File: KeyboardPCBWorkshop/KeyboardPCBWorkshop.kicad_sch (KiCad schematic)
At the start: 1 part, among them U1 ATmega32U4-A

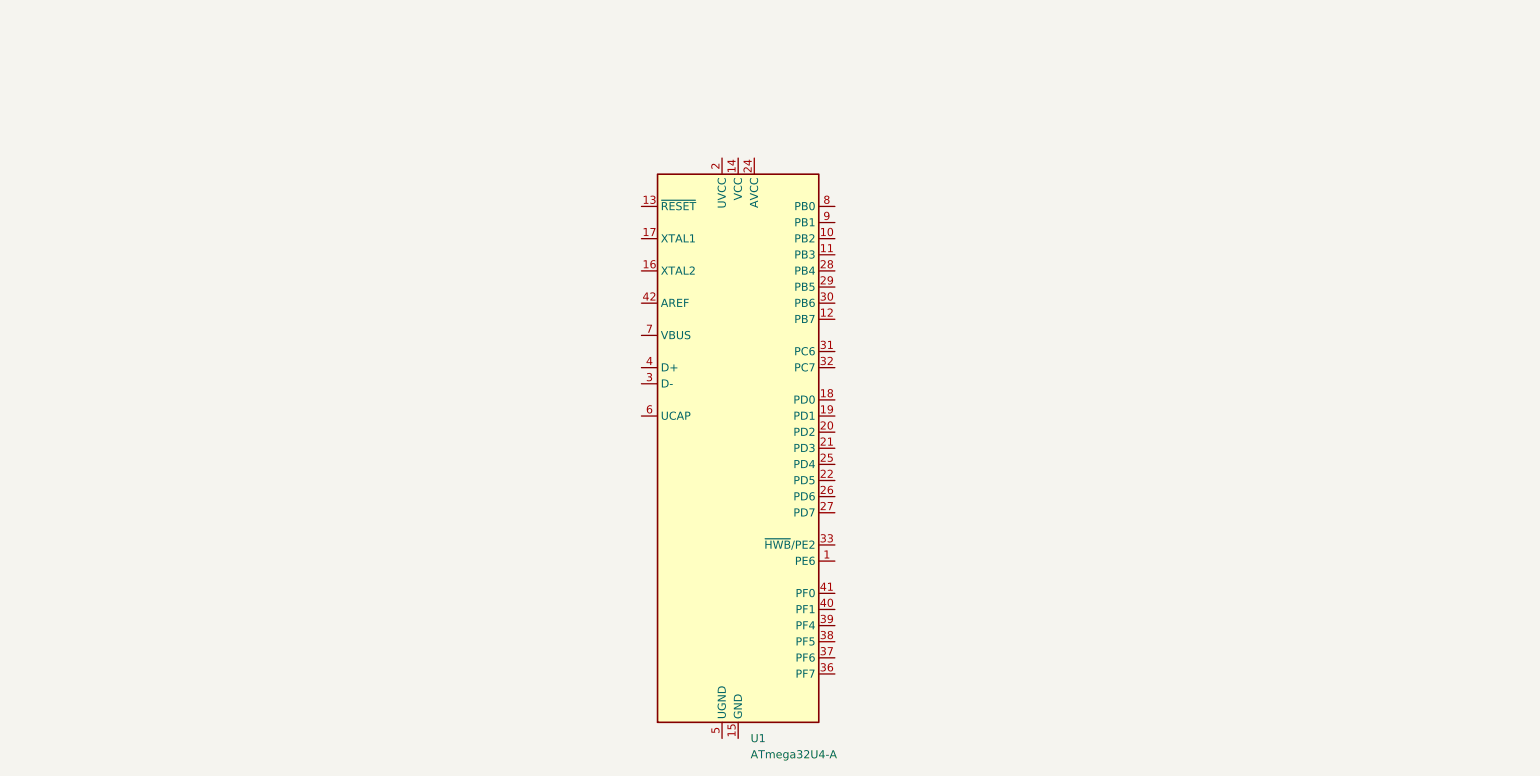
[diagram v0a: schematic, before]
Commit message: added XTAL, coupling cap, ISP header
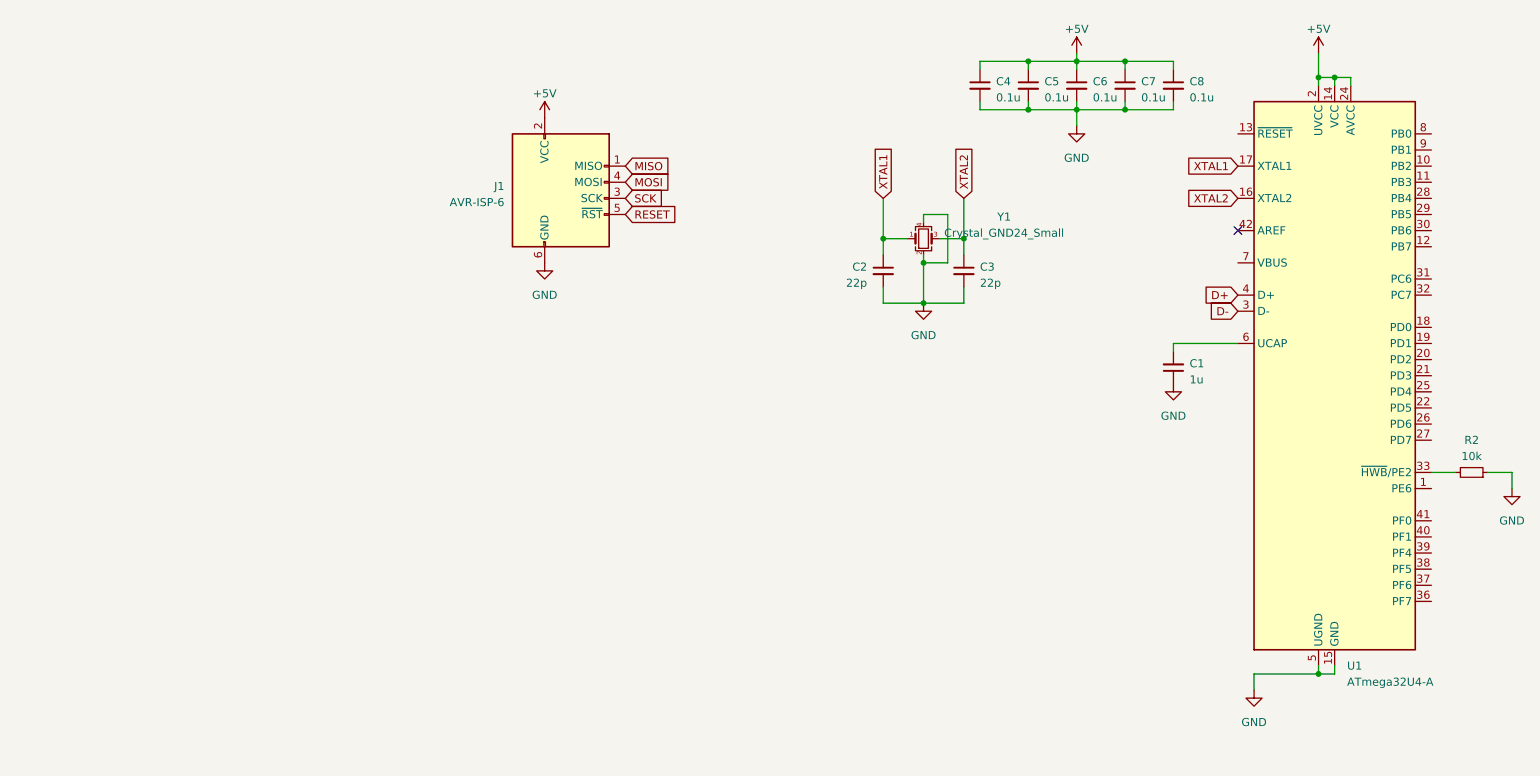
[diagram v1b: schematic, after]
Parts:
- added C1: 1u, symbol Device:C_Small
- added C2, C3: 22p, symbol Device:C_Small
- added C4, C5, C6, C7, C8: 0.1u, symbol Device:C_Small
- added J1: AVR-ISP-6, symbol Connector:AVR-ISP-6
- added R2: 10k, symbol Device:R_Small
- added Y1: Crystal_GND24_Small, symbol Device:Crystal_GND24_Small
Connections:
- net +5V: now reaches U1.14 (VCC), U1.34 (VCC)
- net +5V: now also U1.2 (UVCC), U1.24 (AVCC), U1.44 (AVCC), C4.1, C5.1, C6.1, C7.1, C8.1, J1.2 (VCC)
- net GND: now reaches U1.15 (GND), U1.23 (GND), U1.35 (GND), U1.43 (GND)
- net GND: now also U1.5 (UGND), C1.1, C2.2, C3.2, C4.2, C5.2, C6.2, C7.2, C8.2, J1.6 (GND), R2.1, Y1.2, Y1.4
- net XTAL2: now reaches U1.16 (XTAL2)
- net XTAL2: now also C3.1, Y1.3
- net XTAL1: now reaches U1.17 (XTAL1)
- net XTAL1: now also C2.1, Y1.1
- net D-: now reaches U1.3 (D-)
- net at U1.33 (~{HWB}/PE2): now also R2.2
- net D+: now reaches U1.4 (D+)
- net at U1.6 (UCAP): now also C1.2
- new net MISO: J1.1 (MISO)
- new net MOSI: J1.4 (MOSI)
- new net RESET: J1.5 (~{RST})
- new net SCK: J1.3 (SCK)
- no-connect marks 0 -> 1
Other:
- moved on the sheet: U1

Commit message: Added reset circuit and USB port
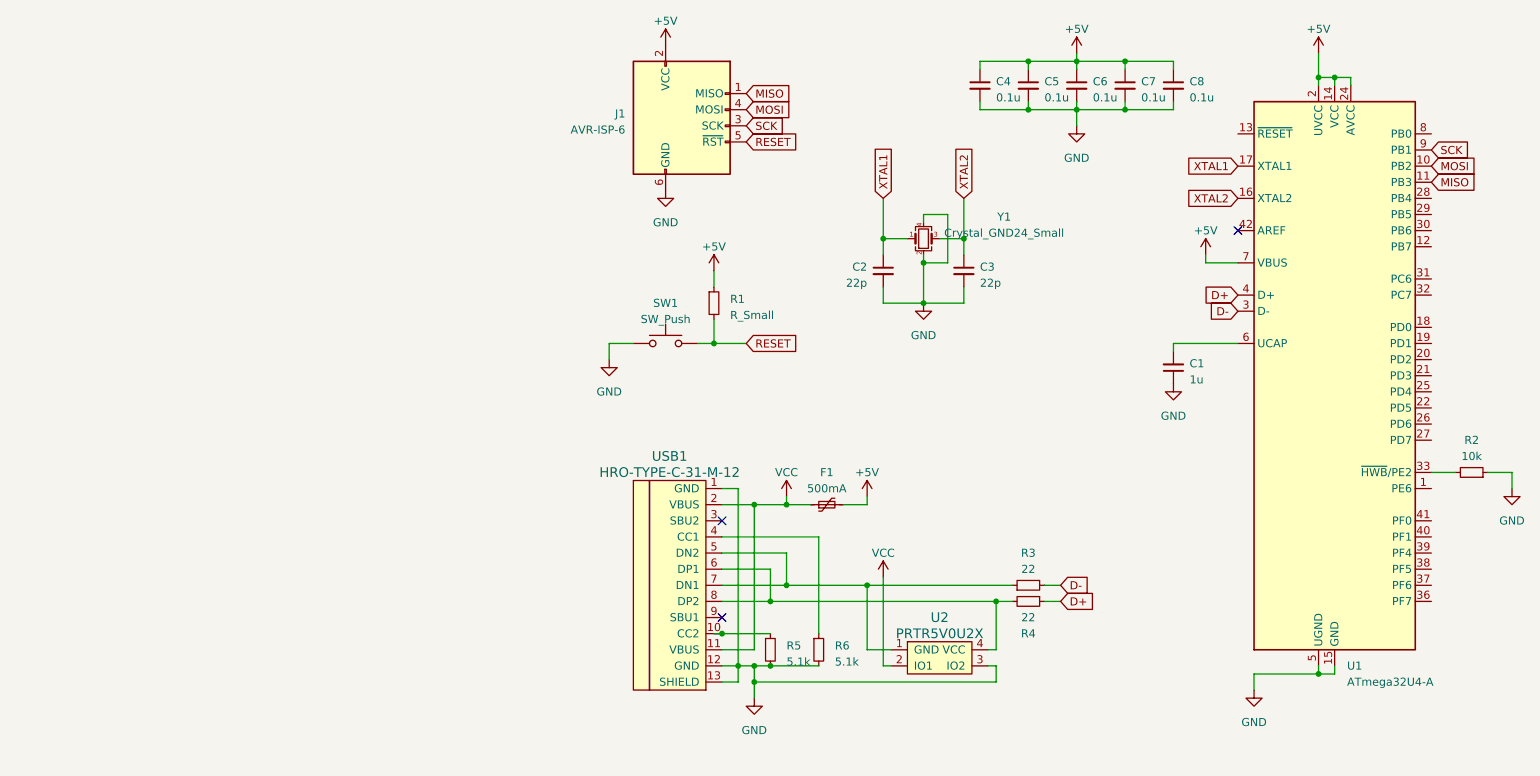
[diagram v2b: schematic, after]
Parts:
- added F1: 500mA, symbol Device:Polyfuse_Small
- added R1: R_Small, symbol Device:R_Small
- added R3, R4: 22, symbol Device:R_Small
- added R5, R6: 5.1k, symbol Device:R_Small
- added SW1: SW_Push, symbol Switch:SW_Push
- added U2: PRTR5V0U2X, symbol random-keyboard-parts:PRTR5V0U2X
- added USB1: HRO-TYPE-C-31-M-12, symbol Type-C:HRO-TYPE-C-31-M-12
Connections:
- net +5V: now also U1.7 (VBUS), F1.2, R1.1
- net D+: now also R4.1
- net D-: now also R3.2
- net GND: now also R5.2, R6.2, SW1.1, U2.3 (IO2), USB1.1 (GND), USB1.12 (GND), USB1.13 (SHIELD)
- net MISO: now also U1.11 (PB3)
- net MOSI: now also U1.10 (PB2)
- net RESET: now also R1.2, SW1.2
- net SCK: now also U1.9 (PB1)
- new net: R5.1, USB1.10 (CC2)
- new net: R6.1, USB1.4 (CC1)
- new net: R3.1, U2.1 (GND), USB1.5 (DN2), USB1.7 (DN1)
- new net: R4.2, U2.4 (VCC), USB1.6 (DP1), USB1.8 (DP2)
- new net VCC: F1.1, U2.2 (IO1), USB1.11 (VBUS), USB1.2 (VBUS)
- no-connect marks 1 -> 3
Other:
- moved on the sheet: J1

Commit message: keyboard matrix
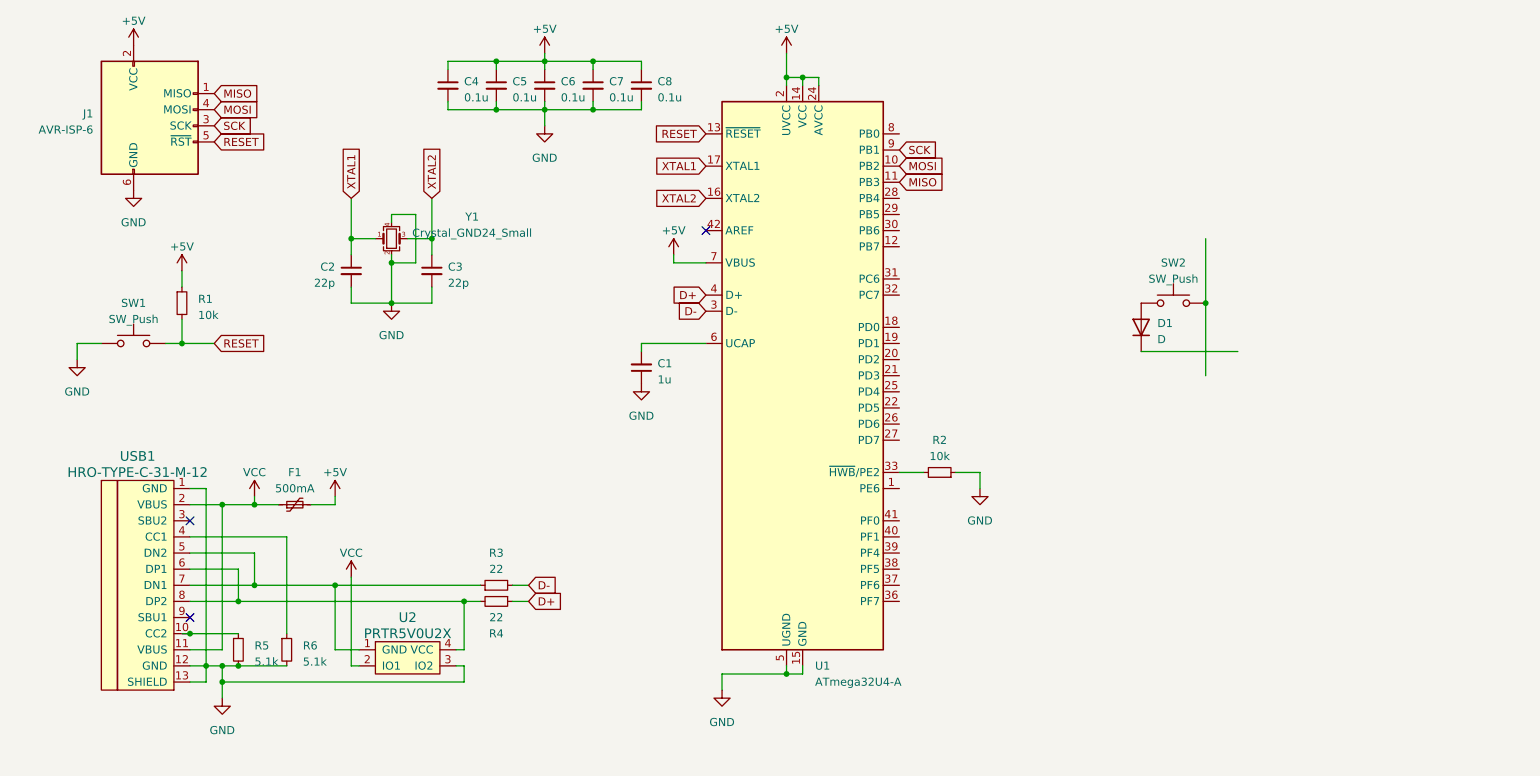
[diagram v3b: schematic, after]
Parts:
- added D1: D, symbol Device:D
- added SW2: SW_Push, symbol Switch:SW_Push
- R1: value R_Small -> 10k
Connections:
- net RESET: now also U1.13 (~{RESET})
- new net: D1.2 (A), SW2.1
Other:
- moved on the sheet: C1, C2, C3, C4, C5, C6, C7, C8, F1, J1, R1, R2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

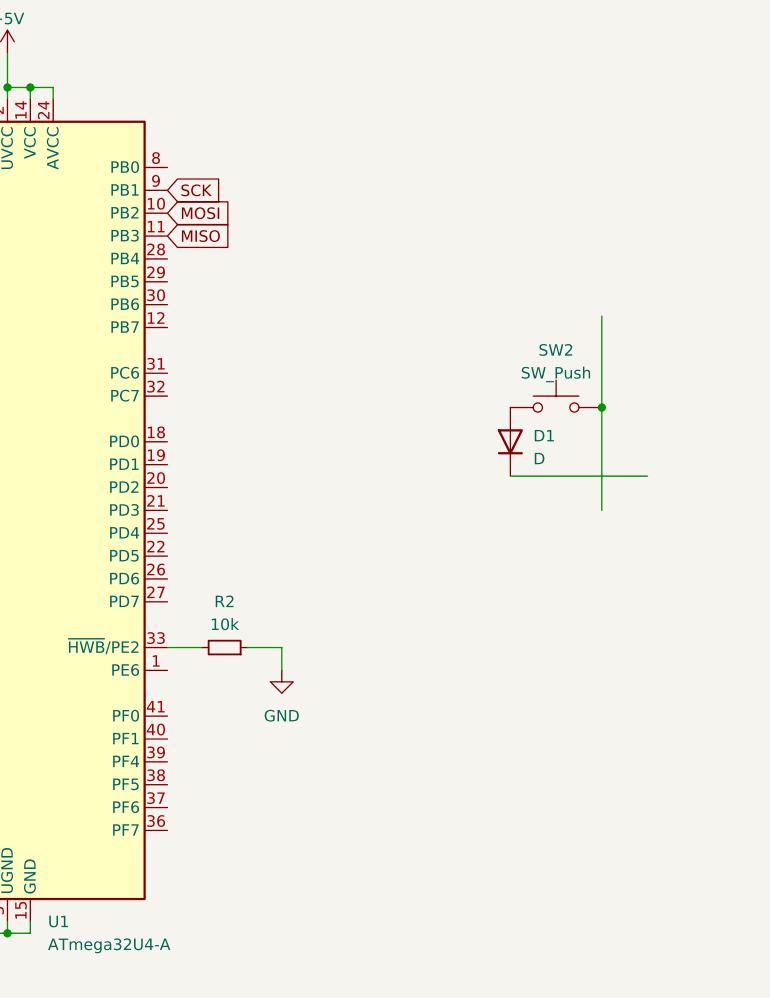
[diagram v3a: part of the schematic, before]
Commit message: completed switch matrices
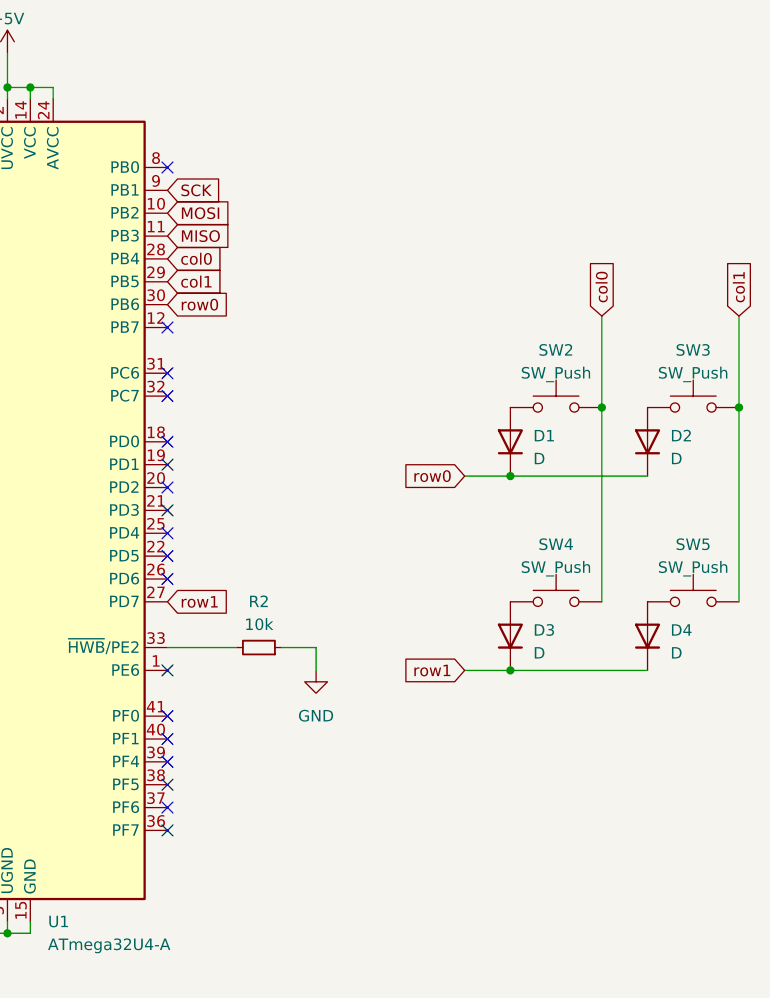
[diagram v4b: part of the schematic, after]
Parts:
- added D2, D3, D4: D, symbol Device:D
- added SW3, SW4, SW5: SW_Push, symbol Switch:SW_Push
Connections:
- net col0: now reaches SW2.2
- net col0: now also U1.28 (PB4), SW4.2
- net row1: now reaches U1.27 (PD7)
- net row1: now also D3.1 (K), D4.1 (K)
- net col1: now reaches U1.29 (PB5)
- net col1: now also SW3.2, SW5.2
- net row0: now reaches U1.30 (PB6)
- net row0: now also D1.1 (K), D2.1 (K)
- new net: D3.2 (A), SW4.1
- new net: D2.2 (A), SW3.1
- new net: D4.2 (A), SW5.1
- no-connect marks 3 -> 21
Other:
- moved on the sheet: R2
